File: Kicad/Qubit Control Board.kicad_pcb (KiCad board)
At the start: 6 copper layers, 64 x 81.5 mm, 150 parts, among them J1 USB_C_Receptacle_PowerOnly_6P, J2 CLK_Pins, J3 Idata, J4 Qdata, J5 SPIdata, J6 SMA, U1 LT3045xMSE, U2 TRF372017IRGZR, U3 LT3045xMSE, U4 LT3045xMSE, U5 SN65LVDS1DBV, U6 AD9743BCPZ, Y2 CVHD-950-100.000

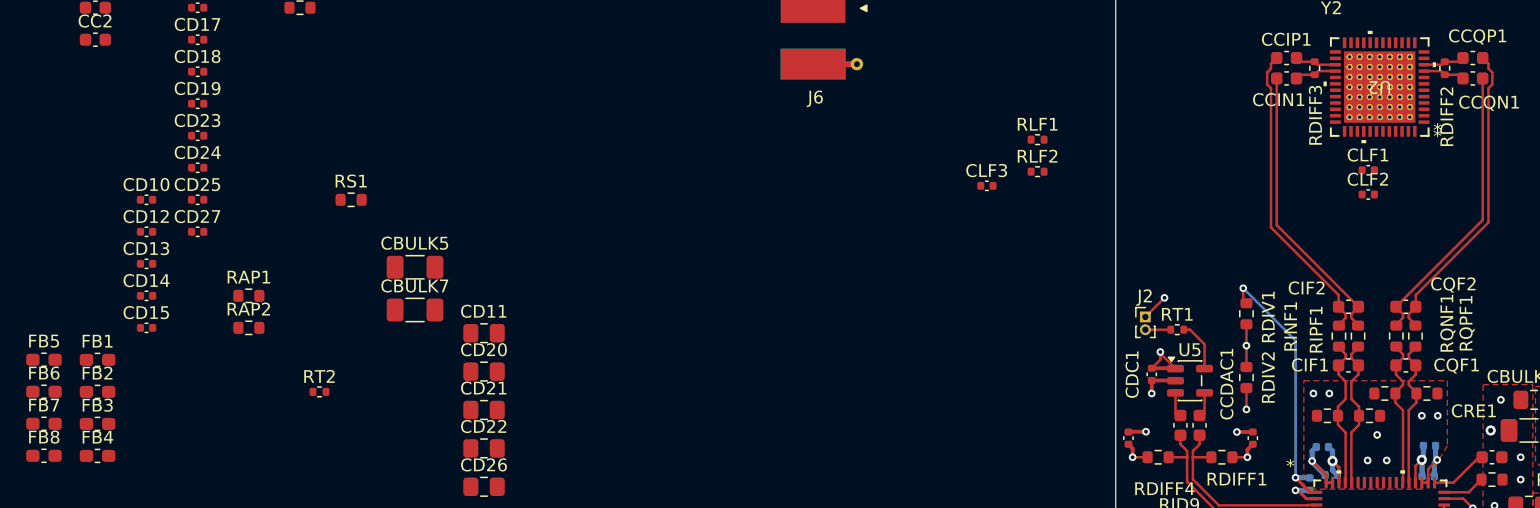
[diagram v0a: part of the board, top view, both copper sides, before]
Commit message: LF routing + power routing for PLL
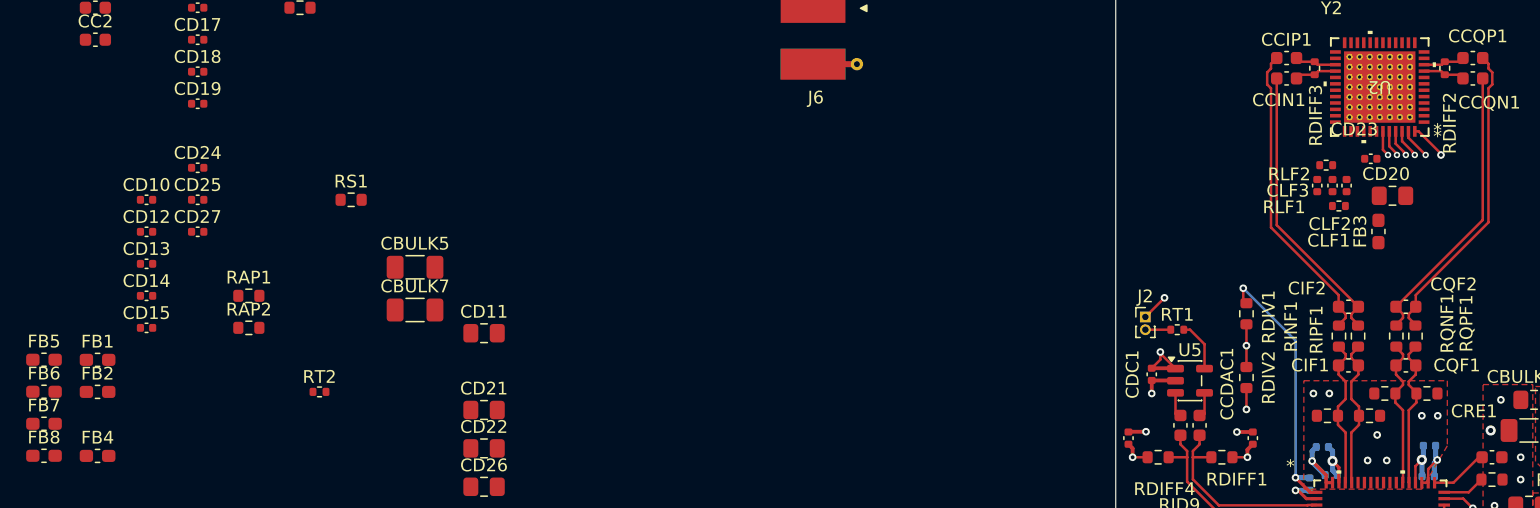
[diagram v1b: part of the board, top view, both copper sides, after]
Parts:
- moved FB3 101.6 mm to (127.1, 73.8), turned to 90 degrees
- moved CD23 92.0 mm to (126.5, 68.1), turned to 180 degrees
- moved CD20 72.5 mm to (128.2, 71.0), turned to 180 degrees
- moved CLF3 25.9 mm to (122.3, 70.2), turned to -90 degrees
- moved RLF1 24.2 mm to (124.0, 71.8), turned to 180 degrees
- moved RLF2 22.6 mm to (123.0, 68.6), turned to 180 degrees
- moved CLF1 3.05 mm to (123.5, 70.2), turned to -90 degrees
- moved CLF2 1.84 mm to (124.6, 70.2), turned to -90 degrees
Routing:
- net GND: track 63.3 -> 68.3 mm, vias 64 -> 66
- net /CLK: track 0.00 -> 2.41 mm, vias 0 -> 1
- net /LE: track 0.00 -> 2.27 mm, vias 0 -> 1
- net /DATA: track 0.00 -> 2.26 mm, vias 0 -> 1
- net /REFIN: track 0.00 -> 2.02 mm, vias 0 -> 1

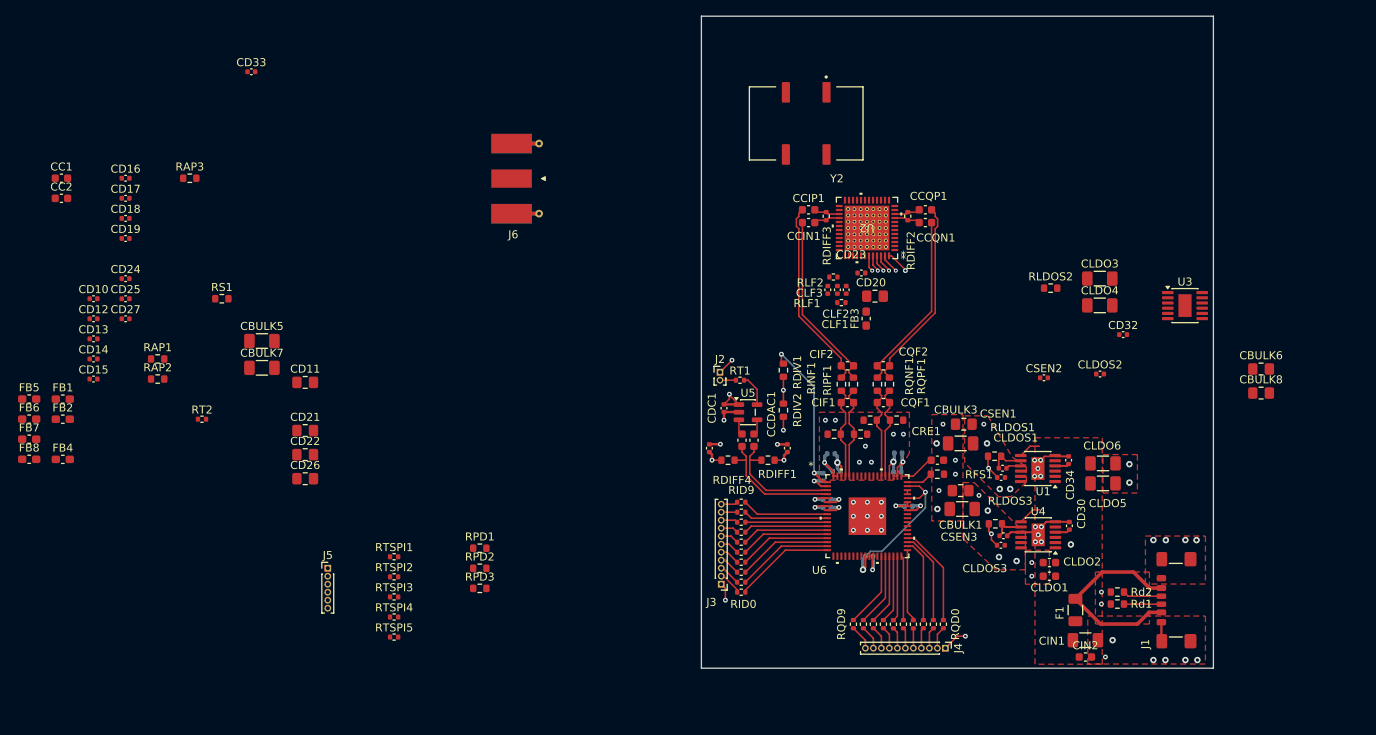
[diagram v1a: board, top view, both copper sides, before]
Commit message: Did 3.3V-B LDO routing
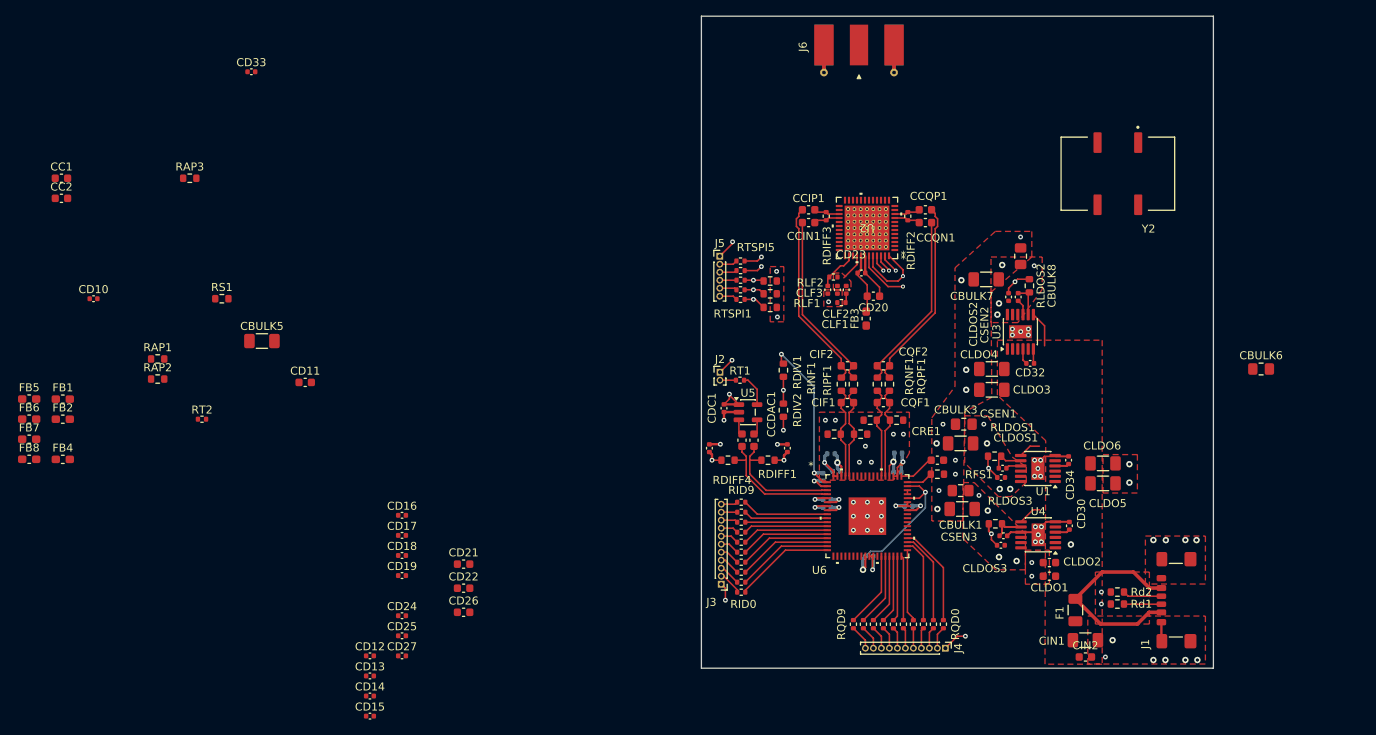
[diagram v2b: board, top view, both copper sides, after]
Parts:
- CD11, CD20, CD21, CD22, CD26: footprint Capacitor_SMD:C_0805_2012Metric_Pad1.18x1.45mm_HandSolder -> Capacitor_SMD:C_0603_1608Metric
- moved CBULK7 91.2 mm to (142.1, 68.9), turned to 180 degrees
- moved RTSPI5 63.9 mm to (111.4, 66.6), turned to 180 degrees
- moved J5 62.6 mm to (108.8, 66.0)
- moved RTSPI4 61.2 mm to (111.4, 67.8), turned to 180 degrees
- moved RTSPI3 58.7 mm to (111.4, 69.0), turned to 180 degrees
- moved RTSPI2 56.2 mm to (111.4, 70.2), turned to 180 degrees
- moved CD17 54.5 mm to (69.1, 100.9)
- moved CD19 54.5 mm to (69.1, 105.9)
- moved CD25 54.5 mm to (69.1, 113.5)
- moved CD13 54.5 mm to (65.1, 118.5)
- moved CD14 54.5 mm to (65.1, 121.0)
- moved CD16 54.5 mm to (69.1, 98.4)
- moved CD18 54.5 mm to (69.1, 103.4)
- moved CD12 54.5 mm to (65.1, 116.0)
- moved CD15 54.5 mm to (65.1, 123.5)
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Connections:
- J5 pad 1: Net-(J5-Pin_1) -> GND
- J5 pad 6: GND -> Net-(J5-Pin_6)
- RTSPI1 pad 2: Net-(J5-Pin_5) -> Net-(J5-Pin_6)
- RTSPI2 pad 2: Net-(J5-Pin_4) -> Net-(J5-Pin_5)
- RTSPI3 pad 2: Net-(J5-Pin_3) -> Net-(J5-Pin_4)
- RTSPI4 pad 2: Net-(J5-Pin_2) -> Net-(J5-Pin_3)
- RTSPI5 pad 2: Net-(J5-Pin_1) -> Net-(J5-Pin_2)
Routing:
- net GND: track 68.3 -> 88.5 mm, vias 66 -> 79
- net /VCC_PLL: track 0.00 -> 7.70 mm
- net +5V: track 9.45 -> 15.9 mm
- net /VTUNE: track 0.00 -> 5.11 mm
- net /REFIN: track 2.02 -> 6.70 mm
- net Net-(U3-SET): track 0.00 -> 4.28 mm
- net /CP_OUT: track 0.00 -> 3.43 mm
- net /LE: track 2.27 -> 5.06 mm, vias 1 -> 2
- net /DATA: track 2.26 -> 4.85 mm, vias 1 -> 2
- net /CLK: track 2.41 -> 4.82 mm, vias 1 -> 2
- net /RDBK: track 0.00 -> 2.31 mm, vias 0 -> 1
- net /LD: track 0.00 -> 2.30 mm, vias 0 -> 1
- net Net-(J5-Pin_6): track 0.00 -> 2.25 mm
- net Net-(J5-Pin_2): track 0.00 -> 2.25 mm
- net Net-(J5-Pin_3): track 0.00 -> 2.17 mm
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- added copper zone on F.Cu, net +3.3V-B
- added copper zone on F.Cu, net /CP_OUT

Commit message: SPI control and power routing
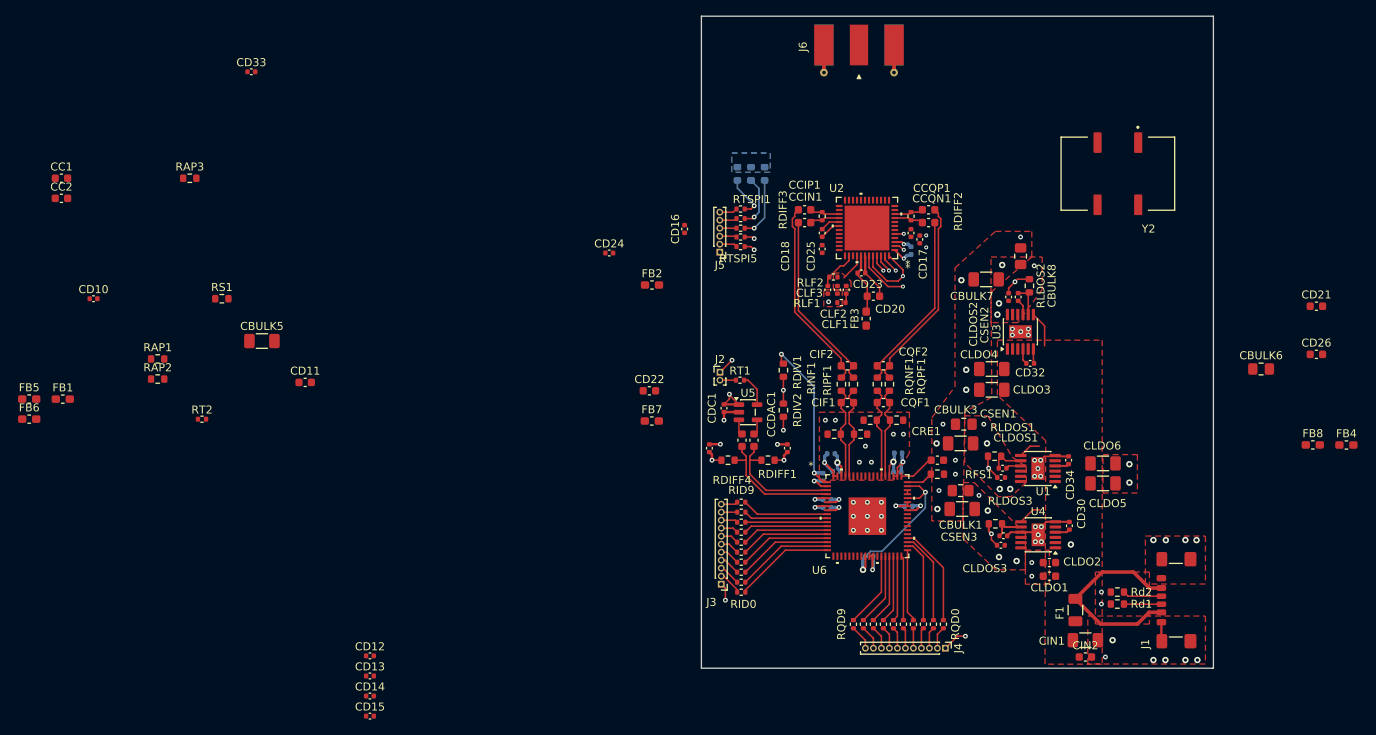
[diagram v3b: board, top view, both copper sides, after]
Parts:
- CD27, RPD1, RPD2, RPD3: moved to B.Cu
- moved FB8 160.5 mm to (182.9, 89.6)
- moved FB4 160.5 mm to (187.1, 89.6)
- moved CD21 111.4 mm to (183.4, 72.2)
- moved CD26 111.4 mm to (183.4, 78.3)
- moved CD27 81.3 mm to (132.7, 65.3), turned to 90 degrees
- moved FB7 77.9 mm to (100.3, 86.6)
- moved CD19 76.7 mm to (132.7, 63.1), turned to -90 degrees
- moved FB2 75.5 mm to (100.3, 69.6)
- moved CD17 74.5 mm to (133.8, 63.9), turned to -90 degrees
- moved CD25 71.4 mm to (121.6, 65.1), turned to 90 degrees
- moved CD18 66.2 mm to (121.6, 63.1), turned to -90 degrees
- moved CD24 52.2 mm to (95.0, 65.6)
- moved CD16 50.3 mm to (104.4, 62.6), turned to 90 degrees
- moved CD22 33.9 mm to (100.0, 82.8)
- moved RPD3 17.2 mm to (111.0, 55.7), turned to -90 degrees
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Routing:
- net /CLK: track 4.82 -> 10.1 mm
- net /DATA: track 4.85 -> 8.77 mm
- net GND: track 88.5 -> 91.2 mm
- net /VCC_LO2: track 0.00 -> 2.69 mm
- net /LE: track 5.06 -> 7.67 mm
- net /VCC_DIG: track 0.00 -> 2.27 mm, vias 0 -> 1
- net Net-(U2-BBI_P): track 3.27 -> 3.77 mm
- net Net-(U2-BBI_N): track 3.29 -> 3.79 mm
- net /RDBK: track 2.31 -> 2.68 mm, vias 1 -> 2
- net /LD: track 2.30 -> 2.41 mm, vias 1 -> 2
- added copper zone on B.Cu, net GND

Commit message: Added 10n input caps to PLL power rails
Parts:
- CD27: moved to F.Cu
- moved CD24 26.7 mm to (121.6, 67.1), turned to 90 degrees
- moved RLF2 0.20 mm to (123.2, 68.6)
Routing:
- net GND: track 91.2 -> 99.4 mm, vias 79 -> 78
- net /VCC_LO1: track 0.00 -> 4.94 mm, vias 0 -> 1
- net /VCC_VCO1: track 0.00 -> 3.10 mm
- net /VCC_VCO2: track 0.00 -> 2.70 mm

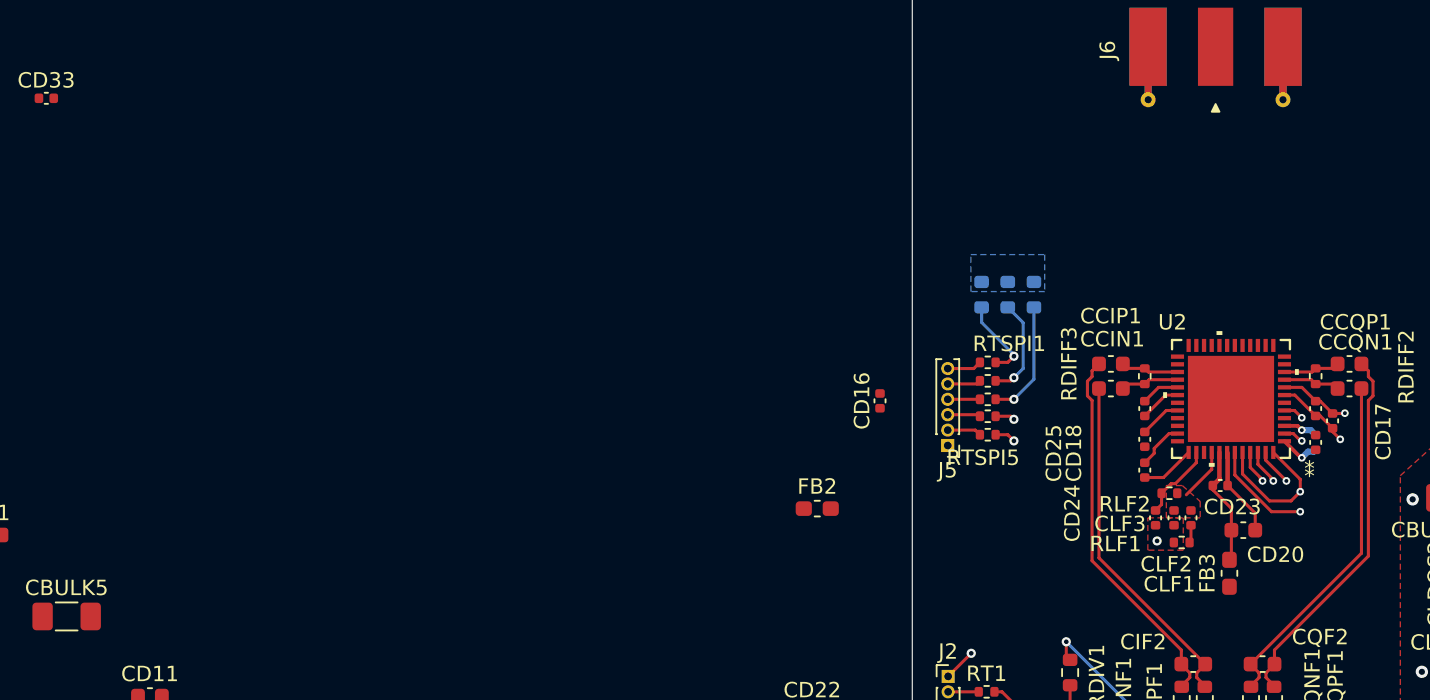
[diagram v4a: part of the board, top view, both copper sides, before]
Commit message: added series R to FB to add damping to oss
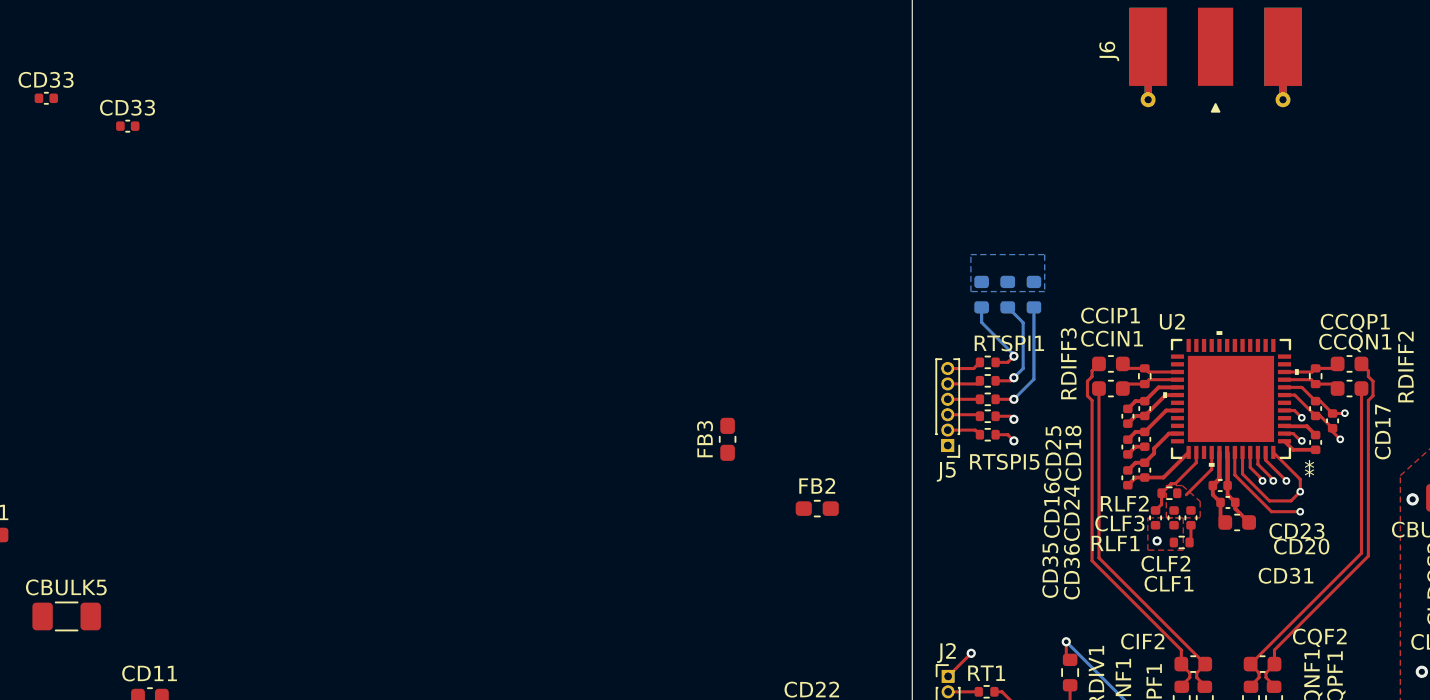
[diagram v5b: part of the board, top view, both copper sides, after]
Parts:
- added CD31: 10n, Capacitor_SMD:C_0402_1005Metric, F.Cu at (127.0, 69.2)
- added CD33: 10n, Capacitor_SMD:C_0402_1005Metric, F.Cu at (55.5, 44.8)
- added CD35: 10n, Capacitor_SMD:C_0402_1005Metric, F.Cu at (120.5, 65.6)
- added CD36: 10n, Capacitor_SMD:C_0402_1005Metric, F.Cu at (120.5, 67.6)
- moved FB3 33.7 mm to (94.5, 65.1)
- moved CD16 16.1 mm to (120.5, 63.6), turned to -90 degrees
- moved CD20 0.64 mm to (127.6, 70.5)
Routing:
- net GND: track 99.4 -> 102.2 mm, vias 78 -> 77
- net /VCC_PLL: track 7.70 -> 5.06 mm
- net /VCC_VCO1: track 3.10 -> 4.40 mm
- net /VCC_LO2: track 2.69 -> 3.99 mm
- net /VCC_VCO2: track 2.70 -> 4.01 mm
- net /VCC_DIG: vias 1 -> 0
